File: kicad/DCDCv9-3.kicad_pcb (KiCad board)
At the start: 4 copper layers, 85.6 x 54 mm, 215 parts, among them J1 Screw_Terminal_01x03, J2 Conn_01x02_Male, J3 Conn_01x02, J4 Conn_01x02_Male, J5 XT60 Male, J6 Conn_01x02_Male, J7 Conn_01x02_Male, J8 Conn_01x02_Male, Q1 PMV20ENR, Q10 IMBG65R050M2HXTMA1, Q11 IMBG65R050M2HXTMA1, Q2 PMV20ENR, Q3 SIHP24N80AE-GE3, Q4 IXYP8N90C3, Q5 PMV20ENR, Q6 PMV20ENR, Q7 PMV20ENR, Q8 BSC027N06LS5ATMA1, Q9 BSC027N06LS5ATMA1, T1 DIY Transformer ETD 39, U1 TBA 1-1212HI, U10 LM2904BIDDFR, U11 UCC21520DW, U12 UCC25600, U13 ZXRE330ASA-7, U14 LM2904BIDDFR, U2 RT9058-90GVL, U3 MP4541_SOP8-EP, U4 TLV61048DBVR, U5 NCP4305DMTTWG, U6 LM2904BIDDFR, U7 TL431, U8 NCP4305DMTTWG, U9 ACPL-217-50AE

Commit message: Important update: Changed Gate Resistors
R58 and R56 have been changed due to slight overvoltage. Deadtime must be increased to at least 150 ns (turn RV1 CCW). For more details see release notes DCDCv9-3r1.3
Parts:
- R56, R58: value 4.7 -> 10
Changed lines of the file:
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@@
 			)
 		)
-		(property "comment" ""
+		(property "comment" "If not available, use PD01S1212A https://www.mouser.de/ProductDetail/Delta-Electronics/PD01S1212A?qs=%2FW4LtXOBxKsNNDIpmtt%2FbQ%3D%3D "
 			(at 0 0 180)
 			(unlocked yes)
@@
 			)
 		)
-		(property "Datasheet" "https://www.mouser.de/ProductDetail/Murata-Electronics/GRM188C61E226ME01J?qs=Z%252BL2brAPG1Ka41zYia00qA%3D%3D"
+		(property "Datasheet" "https://www.mouser.de/ProductDetail/Samsung-Electro-Mechanics/CL21A226MAYNNNE?qs=xZ%2FP%252Ba9zWqY%2FVvCfXjMhqg%3D%3D"
 			(at 0 0 180)
 			(unlocked yes)
@@
 			)
 		)
-		(property "Manufacturer_Part_Number" "GRM188C61E226ME01J"
+		(property "Manufacturer_Part_Number" "CL21A226MAYNNNE"
 			(at 0 0 180)
 			(unlocked yes)
@@
 			)
 		)
-		(property "Datasheet" "https://www.mouser.de/ProductDetail/Murata-Electronics/GRM188C61E226ME01J?qs=Z%252BL2brAPG1Ka41zYia00qA%3D%3D"
+		(property "Datasheet" "https://www.mouser.de/ProductDetail/Samsung-Electro-Mechanics/CL21A226MAYNNNE?qs=xZ%2FP%252Ba9zWqY%2FVvCfXjMhqg%3D%3D"
 			(at 0 0 90)
 			(unlocked yes)
@@
 			)
 		)
-		(property "Manufacturer_Part_Number" "GRM188C61E226ME01J"
+		(property "Manufacturer_Part_Number" "CL21A226MAYNNNE"
 			(at 0 0 90)
 			(unlocked yes)
@@
 			)
 		)
-		(property "Datasheet" "https://www.mouser.de/ProductDetail/Murata-Electronics/GRM188C61E226ME01J?qs=Z%252BL2brAPG1Ka41zYia00qA%3D%3D"
+		(property "Datasheet" "https://www.mouser.de/ProductDetail/Samsung-Electro-Mechanics/CL21A226MAYNNNE?qs=xZ%2FP%252Ba9zWqY%2FVvCfXjMhqg%3D%3D"
 			(at 0 0 180)
 			(unlocked yes)
@@
 			)
 		)
-		(property "Manufacturer_Part_Number" "GRM188C61E226ME01J"
+		(property "Manufacturer_Part_Number" "CL21A226MAYNNNE"
 			(at 0 0 0)
 			(unlocked yes)
@@
 			)
 		)
-		(property "Datasheet" "https://www.mouser.de/ProductDetail/Murata-Electronics/GRM188C61E226ME01J?qs=Z%252BL2brAPG1Ka41zYia00qA%3D%3D"
+		(property "Datasheet" "https://www.mouser.de/ProductDetail/Samsung-Electro-Mechanics/CL21A226MAYNNNE?qs=xZ%2FP%252Ba9zWqY%2FVvCfXjMhqg%3D%3D"
 			(at 0 0 0)
 			(unlocked yes)
@@
 			)
 		)
-		(property "Manufacturer_Part_Number" "GRM188C61E226ME01J"
+		(property "Manufacturer_Part_Number" "CL21A226MAYNNNE"
 			(at 0 0 0)
 			(unlocked yes)
@@
 			)
 		)
-		(property "Value" "4.7"
+		(property "Value" "10"
 			(at 0 -1.82 0)
 			(layer "B.Fab")
@@
 			)
 		)
-		(property "Datasheet" "https://www.mouser.de/ProductDetail/Panasonic/ERJ-P08J4R7V?qs=sGAEpiMZZMtlubZbdhIBIK7FbVYKWV6WtRy9y9o9OQM%3D"
+		(property "Datasheet" "https://www.mouser.de/ProductDetail/YAGEO/RC1206FR-7W10RL?qs=tggtontpCXM7RQCPv1SaRw%3D%3D"
 			(at 0 0 0)
 			(unlocked yes)
@@
 			)
 		)
-		(property "Manufacturer_Part_Number" "ERJ-P08J4R7V"
+		(property "Manufacturer_Part_Number" "RC1206FR-7W10RL"
 			(at 0 0 180)
 			(unlocked yes)
@@
 			)
 		)
-		(property "Datasheet" "https://www.mouser.de/ProductDetail/Murata-Electronics/GRM188C61E226ME01J?qs=Z%252BL2brAPG1Ka41zYia00qA%3D%3D"
+		(property "Datasheet" "https://www.mouser.de/ProductDetail/Samsung-Electro-Mechanics/CL21A226MAYNNNE?qs=xZ%2FP%252Ba9zWqY%2FVvCfXjMhqg%3D%3D"
 			(at 0 0 -90)
 			(unlocked yes)
@@
 			)
 		)
-		(property "Manufacturer_Part_Number" "GRM188C61E226ME01J"
+		(property "Manufacturer_Part_Number" "CL21A226MAYNNNE"
 			(at 0 0 90)
 			(unlocked yes)
@@
 			)
 		)
-		(property "Datasheet" "https://www.mouser.de/ProductDetail/Murata-Electronics/GRM188C61E226ME01J?qs=Z%252BL2brAPG1Ka41zYia00qA%3D%3D"
+		(property "Datasheet" "https://www.mouser.de/ProductDetail/Samsung-Electro-Mechanics/CL21A226MAYNNNE?qs=xZ%2FP%252Ba9zWqY%2FVvCfXjMhqg%3D%3D"
 			(at 0 0 180)
 			(unlocked yes)
@@
 			)
 		)
-		(property "Manufacturer_Part_Number" "GRM188C61E226ME01J"
+		(property "Manufacturer_Part_Number" "CL21A226MAYNNNE"
 			(at 0 0 0)
 			(unlocked yes)
@@
 			)
 		)
-		(property "Value" "4.7"
+		(property "Value" "10"
 			(at 0 -1.82 0)
 			(layer "B.Fab")
@@
 			)
 		)
-		(property "Datasheet" "https://www.mouser.de/ProductDetail/Panasonic/ERJ-P08J4R7V?qs=sGAEpiMZZMtlubZbdhIBIK7FbVYKWV6WtRy9y9o9OQM%3D"
+		(property "Datasheet" "https://www.mouser.de/ProductDetail/YAGEO/RC1206FR-7W10RL?qs=tggtontpCXM7RQCPv1SaRw%3D%3D"
 			(at 0 0 0)
 			(unlocked yes)
@@
 			)
 		)
-		(property "Manufacturer_Part_Number" "ERJ-P08J4R7V"
+		(property "Manufacturer_Part_Number" "RC1206FR-7W10RL"
 			(at 0 0 180)
 			(unlocked yes)

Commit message: IMPORTANT NOTICE see #10 and fix in iBom
IMPORTANT NOTICE: There was a complaint about the converter not being rules conform. Due to other personal priorities it might take some weeks to solve the addressed points. There is also the chance of some points unable to be resolved. See #10 for further details.
iBom: There were some components missing in the iBom for PCBA.
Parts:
- added R75: 100k, Resistor_SMD:R_0603_1608Metric, F.Cu at (163.7, 71.8)

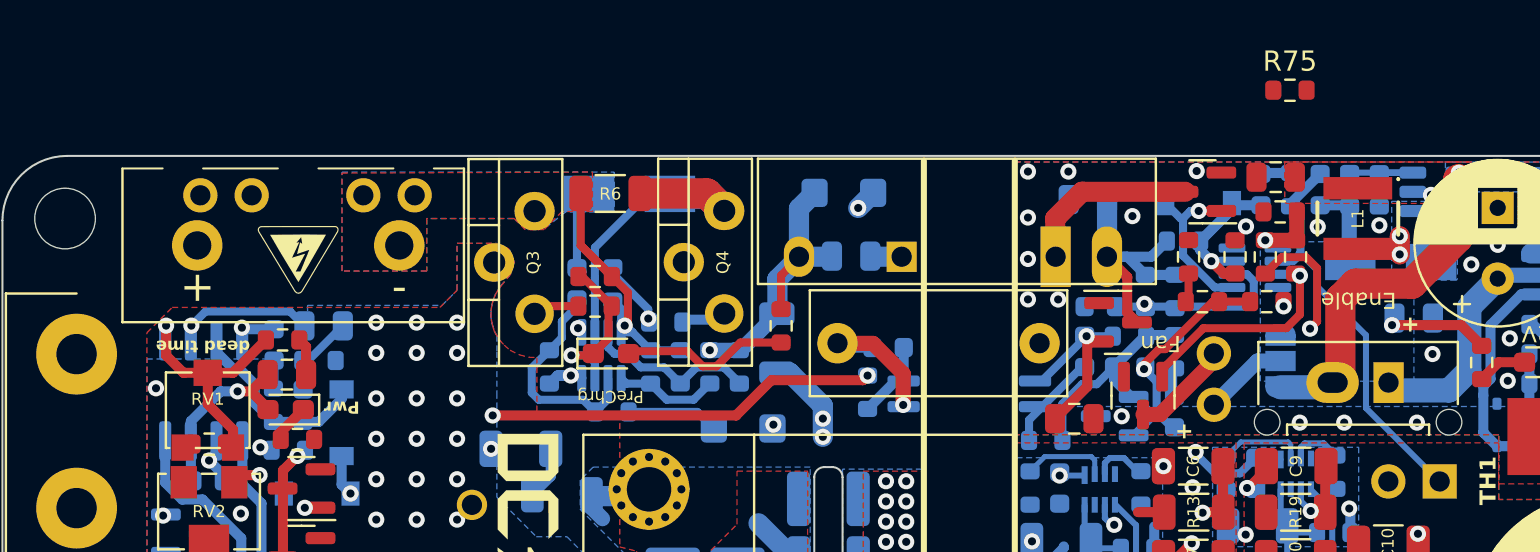
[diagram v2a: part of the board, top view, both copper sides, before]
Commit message: large DCDCv9-3r1.4 release update
- Removed some tables in csv and ods format (xlsx preferred)
- fixed issue #10 (waiting for approval)
- added video of adhesive testing for ESG10C-20G
- added video of primary and secondary winding
- updated all documentation files incl. Scrutineering Support Presentation
- updated transformer isolator part
- updated build notes
- updated README.md
- updated HV input connector
- added note about the discontinuation of the German versions
- added R75 onto the PCB (not required to solder on top of R31 anymore)
- updated iBoms and comments
- removed solder mask between TS an LV for better inspection
- replaced J1, unified crimps for all molex housings
- replaced U1
- fresh production files and gerber PDF plots
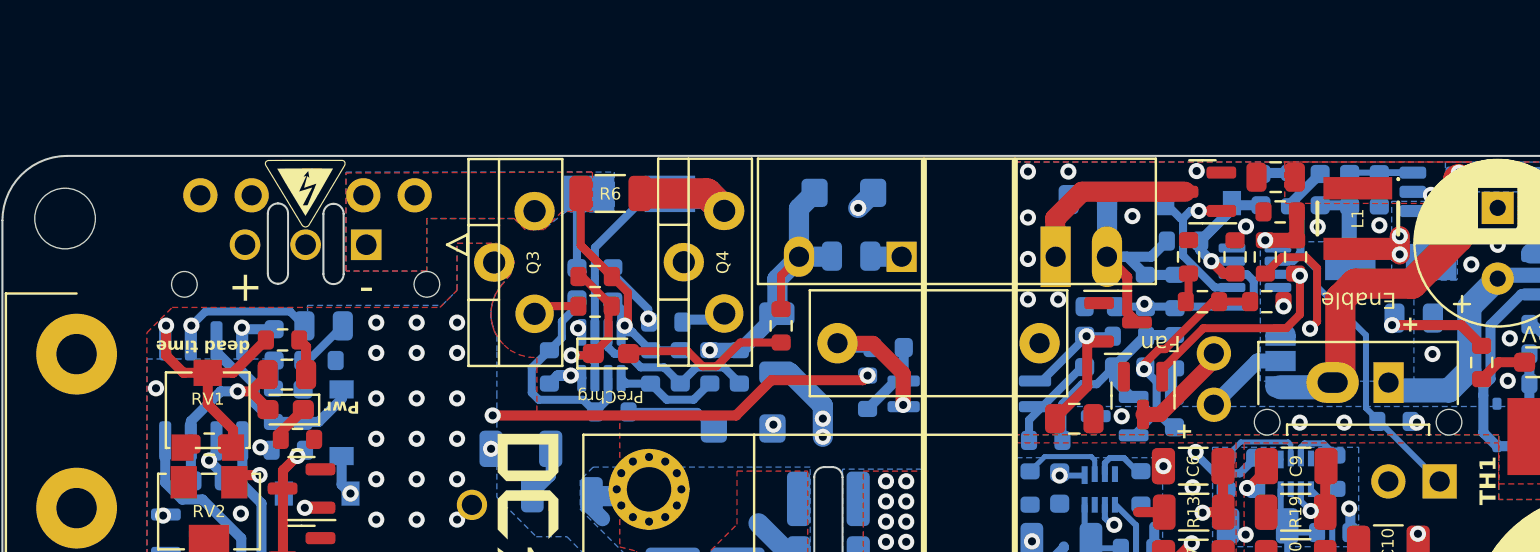
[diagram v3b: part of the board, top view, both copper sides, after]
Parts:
- J1: value Screw_Terminal_01x03 -> 43650-0315; footprint DCDC-Footprints:TerminalBlock_TE-282817-2_1x03_P5.00mm_90 Degrees updated v9-3 -> Samacsys:43650-03YY_151617
- R75: moved to B.Cu
- U1: value TBA 1-1212HI -> RP-1515S
- moved R75 17.2 mm to (168.9, 88.1)
- moved HV_Logo_1 3.29 mm to (115.0, 76.9) (x2)
- moved J1 1.64 mm to (118.0, 79.4), turned to 0 degrees
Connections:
- J1 pad 2: +HV_in -> unconnected-(J1-Pad2)
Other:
- outline, holes or cut-outs redrawn
- board text added: "←"
- board text added: "→"
- board text removed: "←→"

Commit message: Fixed U1 (see Build notes 260410), updated BOMs
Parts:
- U1: value RP-1515S -> RP-1212S
- U7: value TL431 -> TL431BCDBZR
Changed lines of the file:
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@@
 	(paper "A4")
 	(title_block
-		(date "2025-01-26")
+		(date "2026-05-11")
 	)
 	(layers
@@
 			)
 		)
-		(property "Value" "RP-1515S"
+		(property "Value" "RP-1212S"
 			(at 6.5 6.5 0)
 			(layer "F.Fab")
@@
 			)
 		)
-		(property "Datasheet" "https://www.mouser.de/ProductDetail/RECOM-Power/RP-1515S?qs=8OBu2JtKQqqZy6hEc5gvsA%3D%3D"
+		(property "Datasheet" "https://www.mouser.de/ProductDetail/RECOM-Power/RP-1212S?qs=YWgezujkI1KjTZkjNYMtQA%3D%3D"
 			(at 0 0 180)
 			(unlocked yes)
@@
 			)
 		)
-		(property "Manufacturer_Part_Number" "RP-1515S"
+		(property "Manufacturer_Part_Number" "RP-1212S"
 			(at 0 0 180)
 			(unlocked yes)
@@
 			)
 		)
-		(property "Value" "TL431"
+		(property "Value" "TL431BCDBZR"
 			(at 0 -2.4 0)
 			(layer "B.Fab")
